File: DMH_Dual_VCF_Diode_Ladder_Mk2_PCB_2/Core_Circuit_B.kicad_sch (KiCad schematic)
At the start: 41 parts, among them J20 Conn_01x04_PinHeader, SW4 SW_SPDT, SW5 SW_SPDT, SW6 SW_SPDT, U4 TL074, U6 TL074

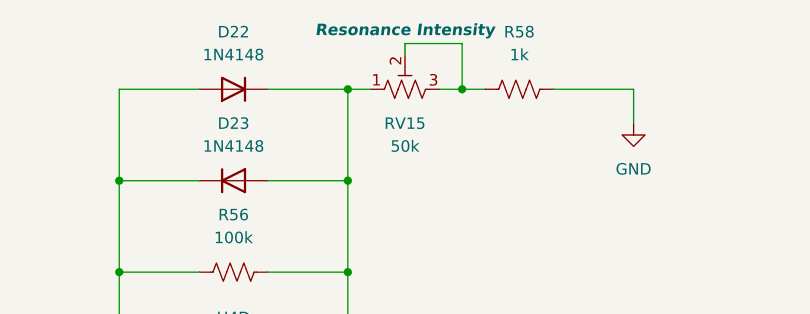
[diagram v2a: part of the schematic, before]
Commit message: Adjusted pin header connections
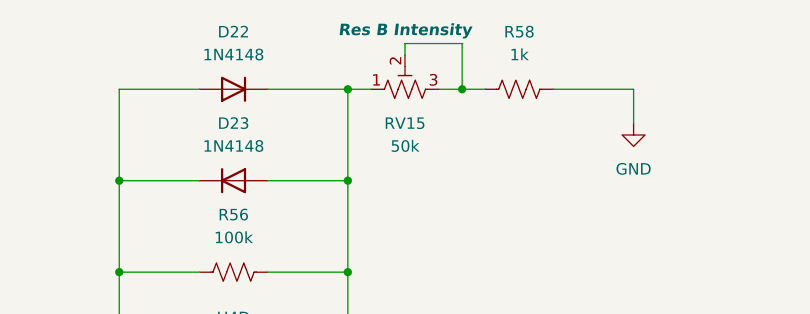
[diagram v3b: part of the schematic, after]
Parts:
- RV15: Function Resonance Intensity -> Res B Intensity
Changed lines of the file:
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@@
 			)
 		)
-		(property "Function" "Resonance Intensity"
+		(property "Function" "Res B Intensity"
 			(at 209.55 23.876 90)
 			(effects

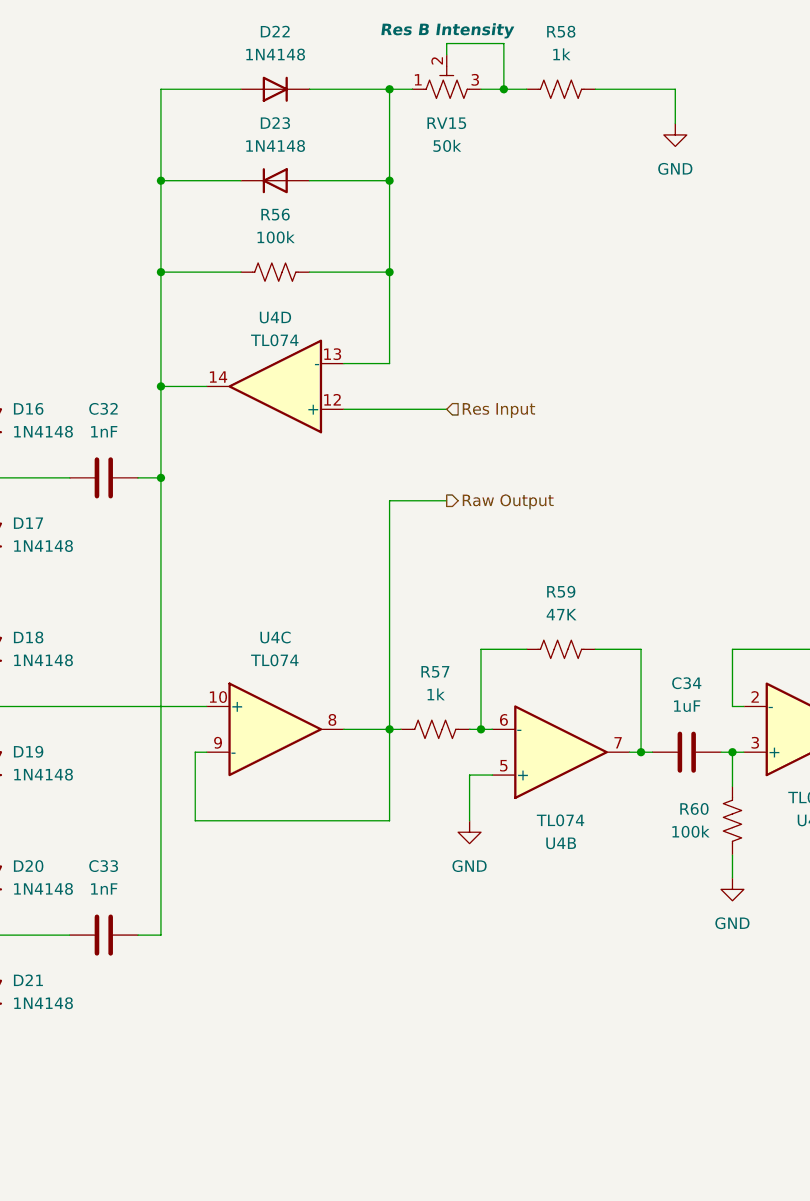
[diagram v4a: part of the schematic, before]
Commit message: Synchronized changes from PCB 1 to PCB 2 schematic
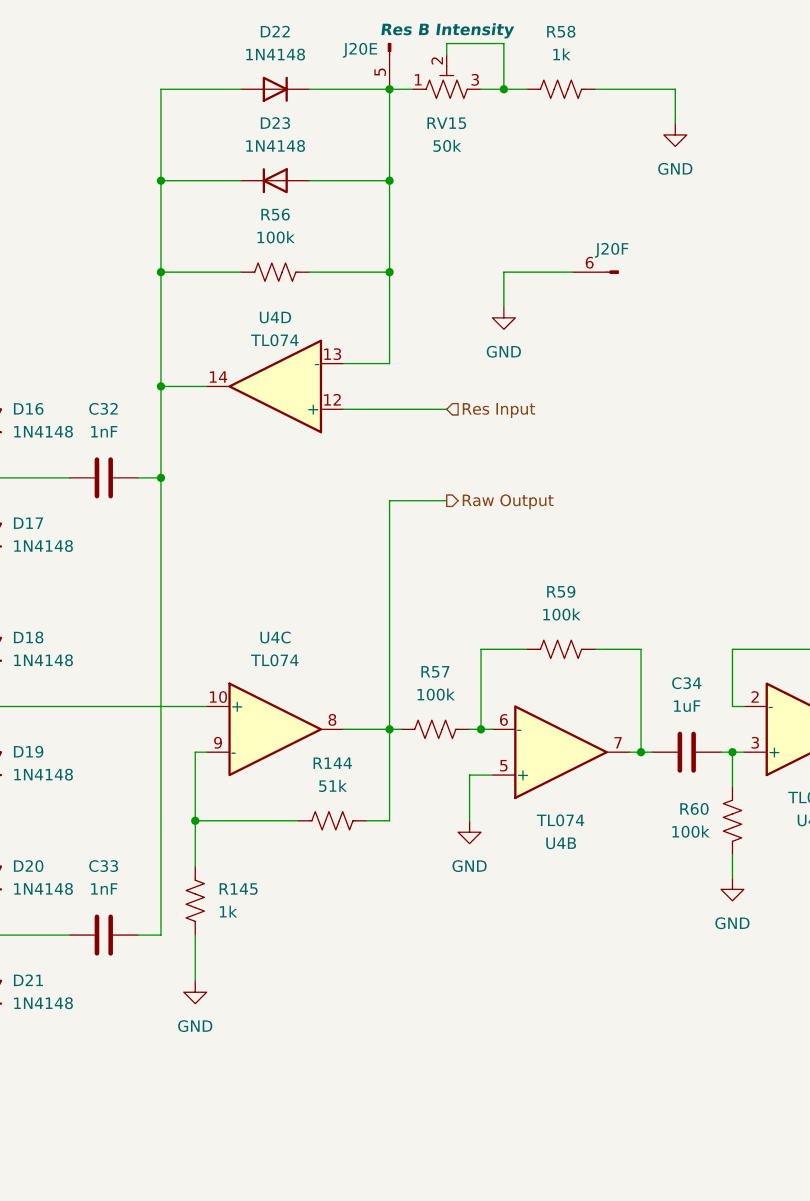
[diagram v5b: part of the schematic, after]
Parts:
- added unit 6 of J20
- added unit 5 of J20
- added R144: 51k, Resistor_THT:R_Axial_DIN0207_L6.3mm_D2.5mm_P7.62mm_Horizontal, symbol Device:R_US
- added R145: 1k, Resistor_THT:R_Axial_DIN0207_L6.3mm_D2.5mm_P7.62mm_Horizontal, symbol Device:R_US
- J20: value Conn_01x04_PinHeader -> Conn_01x06_PinHeader; footprint Connector_PinSocket_2.54mm:PinSocket_1x04_P2.54mm_Vertical -> Connector_PinSocket_2.54mm:PinSocket_1x06_P2.54mm_Vertical; symbol SynthStuff:Conn_01x04_PinHeader -> SynthStuff:Conn_01x06_PinHeader
- R57: value 1k -> 100k
- R59: value 47K -> 100k
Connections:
- net GND: now also J20.6 (Pin_6), R145.1
- net Raw Output: now also R144.2; no longer U4.9 (-)
- net at D22.1 (K), D23.2 (A), R56.2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: now also J20.5 (Pin_5)
- new net: R144.1, R145.2, U4.9 (-)
